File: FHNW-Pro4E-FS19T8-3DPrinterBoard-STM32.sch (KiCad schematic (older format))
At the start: 8 parts, among them J101 Screw_Terminal_01x02, U101 LM2675M-3.3

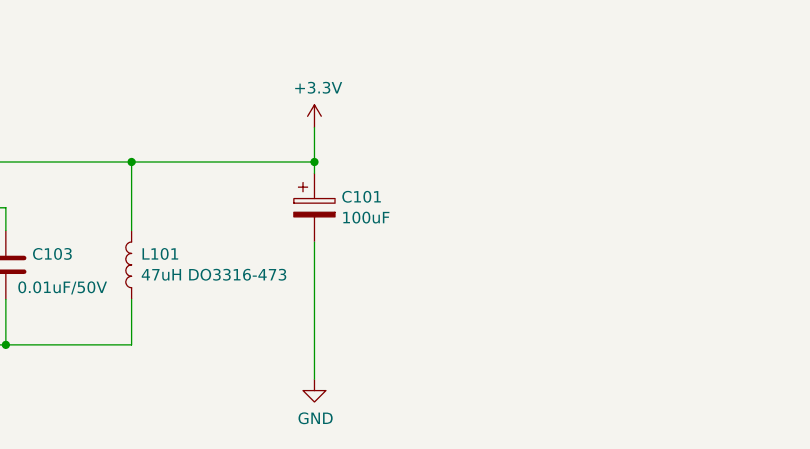
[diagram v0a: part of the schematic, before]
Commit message: added LEDs
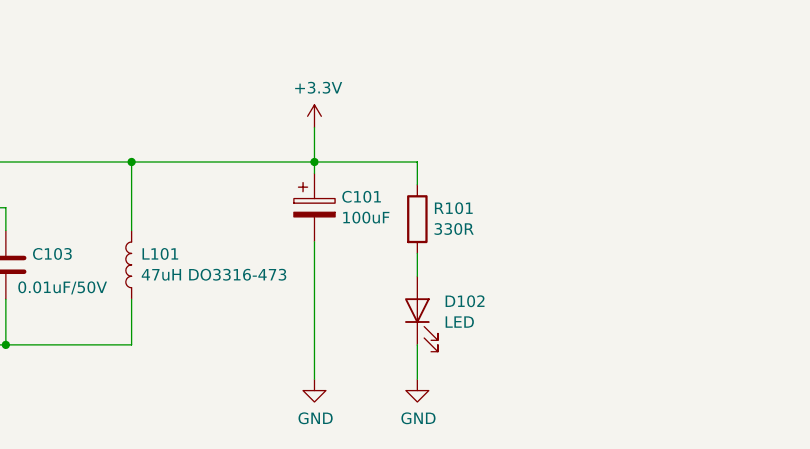
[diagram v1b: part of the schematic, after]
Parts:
- added D102: LED, LED_SMD:LED_0805_2012Metric, symbol Device:LED
- added R101: 330R, Resistors_SMD:R_0603, symbol Device:R
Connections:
- net +3V3: now also R101.1
- net GND: now also D102.1 (K)
- new net: D102.2 (A), R101.2
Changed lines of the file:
@@
 Wire Wire Line
 	2200 7250 2900 7250
+$Comp
+L Device:R R101
+U 1 1 5CB6A127
+P 5400 6700
+F 0 "R101" H 5470 6746 50  0000 L CNN
+F 1 "330R" H 5470 6655 50  0000 L CNN
+F 2 "Resistors_SMD:R_0603" V 5330 6700 50  0001 C CNN
+F 3 "~" H 5400 6700 50  0001 C CNN
+	1    5400 6700
+	1    0    0    -1
+$EndComp
+$Comp
+L Device:LED D102
+U 1 1 5CB6AB63
+P 5400 7100
+F 0 "D102" V 5439 6983 50  0000 R CNN
+F 1 "LED" V 5348 6983 50  0000 R CNN
+F 2 "LED_SMD:LED_0805_2012Metric" H 5400 7100 50  0001 C CNN
+F 3 "~" H 5400 7100 50  0001 C CNN
+	1    5400 7100
+	0    -1   -1   0
+$EndComp
+Wire Wire Line
+	4950 6450 5400 6450
+$Comp
+L power:GND #PWR0141
+U 1 1 5CB6C2A7
+P 5400 7400
+F 0 "#PWR0141" H 5400 7150 50  0001 C CNN
+F 1 "GND" H 5405 7227 50  0000 C CNN
+F 2 "" H 5400 7400 50  0001 C CNN
+F 3 "" H 5400 7400 50  0001 C CNN
+	1    5400 7400
+	1    0    0    -1
+$EndComp
+Wire Wire Line
+	5400 6450 5400 6550
+Wire Wire Line
+	5400 6850 5400 6950
+Wire Wire Line
+	5400 7250 5400 7400
 $EndSCHEMATC

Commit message: corrected P.S. Schematic review
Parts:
- added C104, C105, C106: 100n, Capacitors_SMD:C_0603, symbol Device:C
- added C107: 100uF, Capacitors_SMD:C_1812, symbol Device:CP
- added C108: 330uF, Capacitors_SMD:C_1812, symbol Device:CP
- added C109: 0.01uF/50V, Capacitors_SMD:C_0603, symbol Device:C
- added D103: Shottky STPS1L30A, Diodes_SMD:D_SMB, symbol Device:D_Schottky
- added FB101, FB102: Ferrite, Resistors_SMD:R_0805_HandSoldering, symbol Device:Ferrite_Bead_Small
- added L102: 47uH DO3316-473, Inductors_SMD:L_Fastron_PISN_Handsoldering, symbol Device:L
- added U102: LM2675M-5, Package_SO:SOIC-8_3.9x4.9mm_P1.27mm, symbol Regulator_Switching:LM2675M-5
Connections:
- net labels added: +3.3VA, +3.3VP, 5V
- wire segments 32 -> 74
- no-connect marks 1 -> 0
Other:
- note added: "Layout Datasheet p. 25"

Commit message: fixed missing symbol issue fixed 3vout cap on FTDI
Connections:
- net labels added: +5V
- net labels removed: 5V
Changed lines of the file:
@@
 Wire Wire Line
 	2300 6450 2200 6450
+Text Notes 4250 6000 2    50   ~ 0
+Layout Datasheet p. 25
 $Comp
-L SparkFun-PowerSymbols:5V #SUPPLY0101
-U 1 1 5CC53E98
+L power:+5V #PWR01
+U 1 1 5CBDFC0C
 P 4950 4650
-F 0 "#SUPPLY0101" H 5000 4650 45  0001 L BNN
-F 1 "5V" H 4950 4820 45  0000 C CNN
-F 2 "XXX-00000" H 4950 4831 60  0001 C CNN
-F 3 "" H 4950 4650 60  0001 C CNN
+F 0 "#PWR01" H 4950 4500 50  0001 C CNN
+F 1 "+5V" H 4965 4823 50  0000 C CNN
+F 2 "" H 4950 4650 50  0001 C CNN
+F 3 "" H 4950 4650 50  0001 C CNN
 	1    4950 4650
 	1    0    0    -1
 $EndComp
-Text Notes 4250 6000 2    50   ~ 0
-Layout Datasheet p. 25
 $EndSCHEMATC

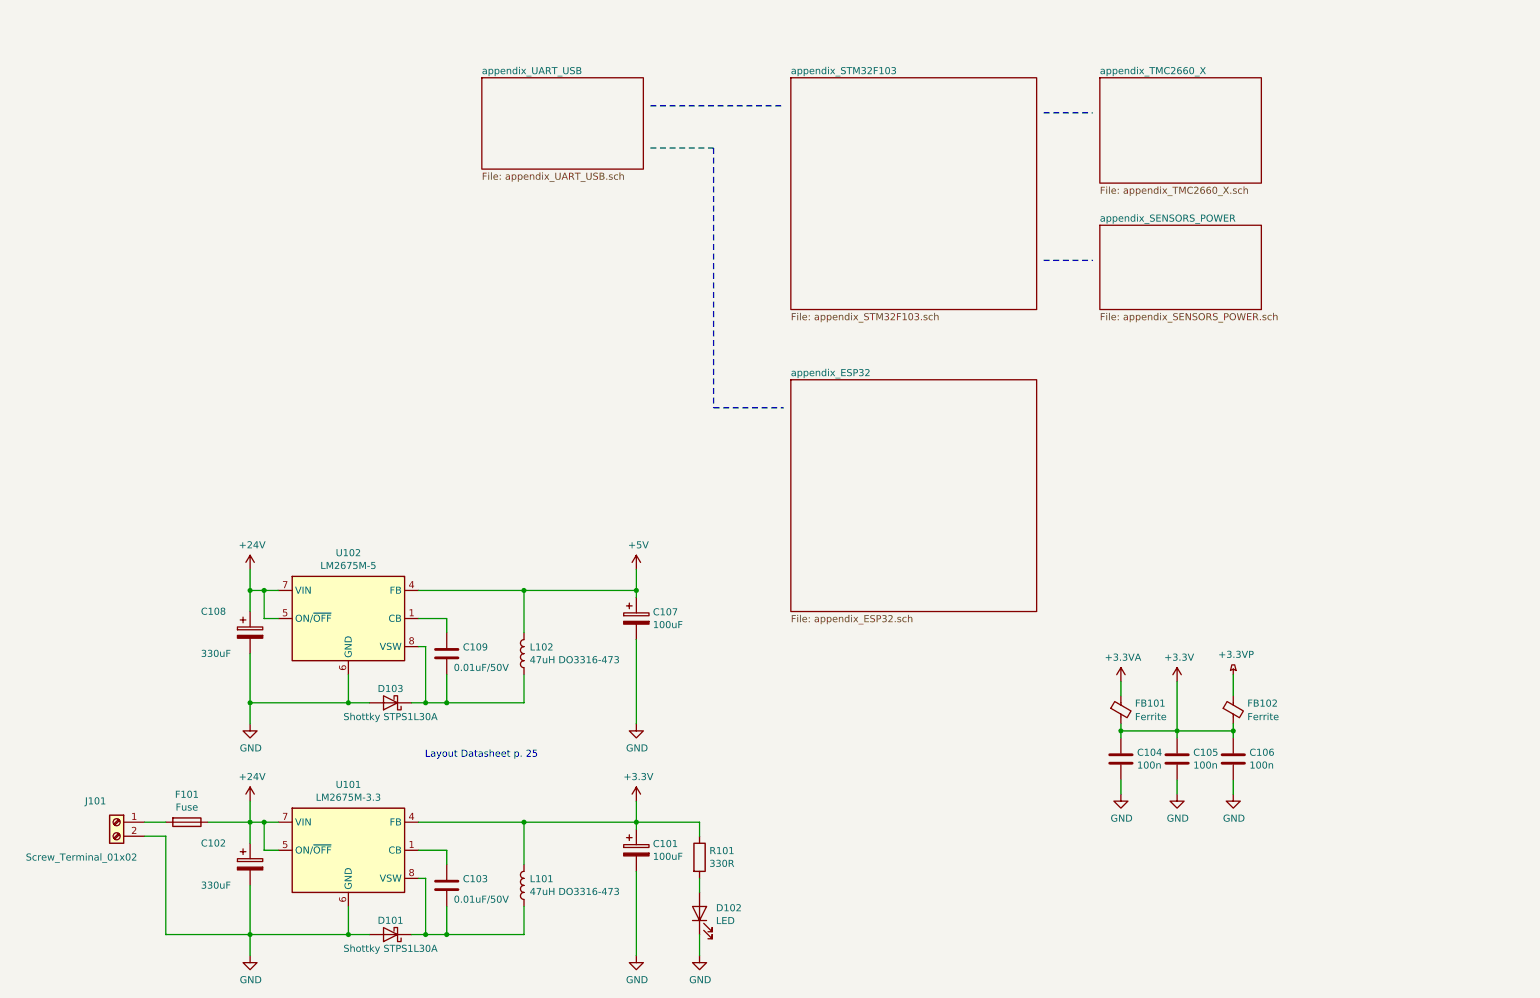
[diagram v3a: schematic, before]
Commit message: started with STM32 Pinout connections (Mittagspause)
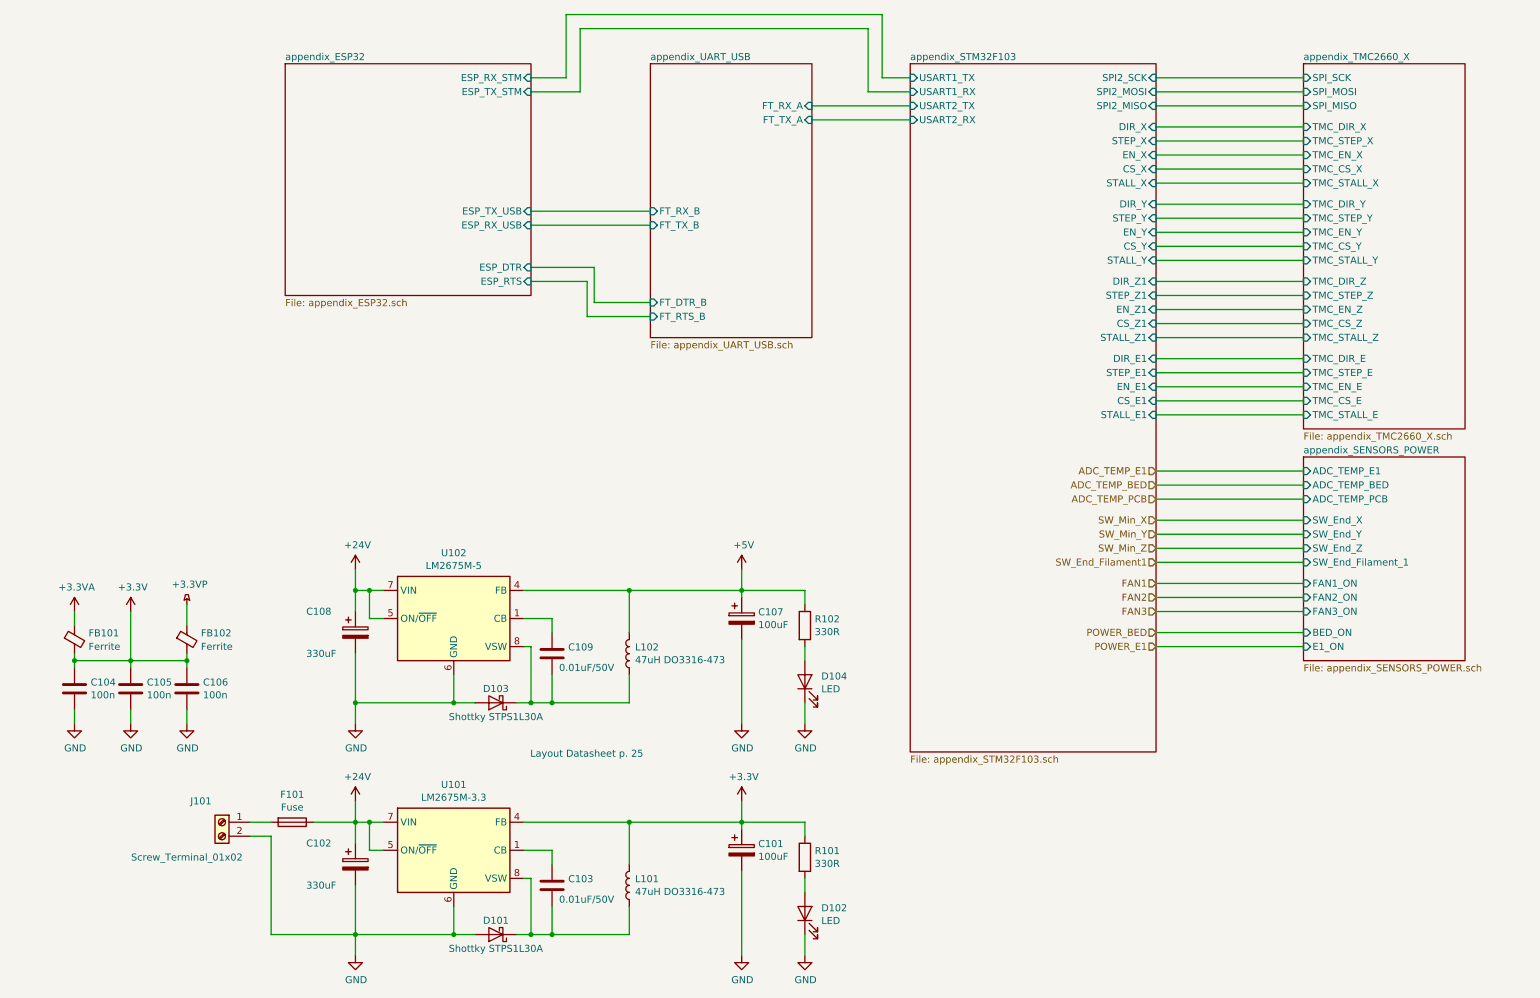
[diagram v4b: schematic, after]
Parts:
- added D104: LED, LED_SMD:LED_0805_2012Metric, symbol Device:LED
- added R102: 330R, Resistors_SMD:R_0603, symbol Device:R
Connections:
- net +5V: now also R102.1
- net GND: now also D104.1 (K)
- new net: D104.2 (A), R102.2
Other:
- moved on the sheet: C101, C102, C103, C104, C105, C106, C107, C108, C109, D101, D102, D103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

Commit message: added cache.lib to git
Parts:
- U101: footprint Housings_SOIC:SOIC-8-1EP_3.9x4.9mm_Pitch1.27mm -> Package_SO:SOIC-8_3.9x4.9mm_P1.27mm
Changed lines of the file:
@@
 F 0 "U101" H 3650 7117 50  0000 C CNN
 F 1 "LM2675M-3.3" H 3650 7026 50  0000 C CNN
-F 2 "Housings_SOIC:SOIC-8-1EP_3.9x4.9mm_Pitch1.27mm" H 3700 6300 50  0001 L CIN
+F 2 "Package_SO:SOIC-8_3.9x4.9mm_P1.27mm" H 3700 6300 50  0001 L CIN
 F 3 "http://www.ti.com/lit/ds/symlink/lm2675.pdf" H 3650 6650 50  0001 C CNN
 	1    3650 6650
@@
 Wire Wire Line
 	6150 5600 6150 5750
-Wire Wire Line
-	4200 2600 4600 2600
-Wire Wire Line
-	4600 2600 4600 2850
-Wire Wire Line
-	4600 2850 5050 2850
 Wire Wire Line
 	5050 2750 4650 2750
@@
 Text HLabel 8650 5200 0    50   Input ~ 0
 POWER_E1
+Wire Wire Line
+	4200 2600 4550 2600
+Wire Wire Line
+	4550 2600 4550 2850
+Wire Wire Line
+	4550 2850 5050 2850
 $EndSCHEMATC

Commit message: Layout update
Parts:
- added H101, H102, H103, H104: MountingHole, Mounting_Holes:MountingHole_3.2mm_M3_Pad, symbol Mechanical:MountingHole
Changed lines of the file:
@@
 Wire Wire Line
 	4550 2850 5050 2850
+$Comp
+L Mechanical:MountingHole H101
+U 1 1 5CBF1F93
+P 850 750
+F 0 "H101" H 950 700 50  0000 L CNN
+F 1 "MountingHole" H 600 600 50  0000 L CNN
+F 2 "Mounting_Holes:MountingHole_3.2mm_M3_Pad" H 850 750 50  0001 C CNN
+F 3 "~" H 850 750 50  0001 C CNN
+	1    850  750
+	1    0    0    -1
+$EndComp
+$Comp
+L Mechanical:MountingHole H102
+U 1 1 5CBF3649
+P 1400 750
+F 0 "H102" H 1500 700 50  0000 L CNN
+F 1 "MountingHole" H 1150 600 50  0000 L CNN
+F 2 "Mounting_Holes:MountingHole_3.2mm_M3_Pad" H 1400 750 50  0001 C CNN
+F 3 "~" H 1400 750 50  0001 C CNN
+	1    1400 750
+	1    0    0    -1
+$EndComp
+$Comp
+L Mechanical:MountingHole H103
+U 1 1 5CBF3A09
+P 850 1050
+F 0 "H103" H 950 1000 50  0000 L CNN
+F 1 "MountingHole" H 600 900 50  0000 L CNN
+F 2 "Mounting_Holes:MountingHole_3.2mm_M3_Pad" H 850 1050 50  0001 C CNN
+F 3 "~" H 850 1050 50  0001 C CNN
+	1    850  1050
+	1    0    0    -1
+$EndComp
+$Comp
+L Mechanical:MountingHole H104
+U 1 1 5CBF3E8E
+P 1400 1050
+F 0 "H104" H 1500 1000 50  0000 L CNN
+F 1 "MountingHole" H 1150 900 50  0000 L CNN
+F 2 "Mounting_Holes:MountingHole_3.2mm_M3_Pad" H 1400 1050 50  0001 C CNN
+F 3 "~" H 1400 1050 50  0001 C CNN
+	1    1400 1050
+	1    0    0    -1
+$EndComp
 $EndSCHEMATC

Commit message: having issues with netclasses
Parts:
- added C110: TBD, Capacitors_SMD:C_0603, symbol Device:C
- added D105: D_Zener, Diodes_SMD:D_SMB, symbol Device:D_Zener
- added R103: TBD, Resistors_SMD:R_0603, symbol Device:R
- added T101: BUK963R3-60E, Package_TO_SOT_SMD:TO-263-2, symbol FHNW-Pro4E-FS19T8-Library:BUK963R3-60E
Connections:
- net GND: now also D105.2 (A), T101.3; no longer J101.2 (Pin_2)
- net at J101.1 (Pin_1): now also T101.2; no longer F101.2
- new net: C110.2, D105.1 (K), R103.2, T101.1
- new net: C110.1, F101.2, J101.2 (Pin_2), R103.1
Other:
- moved on the sheet: C104, C105, C106, FB101, FB102, J101

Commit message: first layout draft without 40pin
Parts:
- added D106: APHBM2012LSURKZGKC, FHNW-Pro4E-FS19T8-Library:LED_Kingbright_SMD4_2.0x1.25, symbol FHNW-Pro4E-FS19T8-Library:APHBM2012LSURKZGKC
- added R104: 10k, Resistors_SMD:R_1206, symbol Device:R
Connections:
- net 24V_GND: now reaches J101.1 (Pin_1), T101.2
- net 24V_GND: now also D106.1 (A1), D106.3 (K2)
- net 24V_IN: now reaches C110.1, F101.2, J101.2 (Pin_2), R103.1
- net 24V_IN: now also R104.1
- new net: D106.2 (K1), D106.4 (A2), R104.2
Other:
- moved on the sheet: J101
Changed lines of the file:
@@
 F27 "CS_E1" I R 8650 3450 50
 F28 "STALL_E1" I R 8650 3550 50
+F29 "ADC_T_E1" I R 8650 3950 50
+F30 "ADC_T_BED" I R 8650 4050 50
+F31 "BED_ON" I R 8650 5100 50
+F32 "E1_ON" I R 8650 5200 50
+F33 "FAN1" I R 8650 4750 50
+F34 "FAN2" I R 8650 4850 50
+F35 "FAN3" I R 8650 4950 50
+F36 "ADC_T_PCB" I R 8650 4150 50
+F37 "SW_Min_X" I R 8650 4300 50
+F38 "SW_Min_Y" I R 8650 4400 50
+F39 "SW_Min_Z1" I R 8650 4500 50
+F40 "SW_Min_Filament1" I R 8650 4600 50
 $EndSheet
 $Sheet
@@
 L Connector:Screw_Terminal_01x02 J101
 U 1 1 5CD68AD6
-P 1250 6550
-F 0 "J101" H 1400 6700 50  0000 C CNN
-F 1 "Screw_Terminal_01x02" H 1500 6300 50  0000 C CNN
-F 2 "Connectors_Terminal_Blocks:TerminalBlock_Altech_AK300-2_P5.00mm" H 1250 6550 50  0001 C CNN
-F 3 "~" H 1250 6550 50  0001 C CNN
-	1    1250 6550
+P 650 6550
+F 0 "J101" H 600 6700 50  0000 C CNN
+F 1 "Screw_Terminal_01x02" V 750 6200 50  0000 C CNN
+F 2 "Connectors_Terminal_Blocks:TerminalBlock_Altech_AK300-2_P5.00mm" H 650 6550 50  0001 C CNN
+F 3 "~" H 650 6550 50  0001 C CNN
+	1    650  6550
 	-1   0    0    1
 $EndComp
@@
 $EndComp
 $Comp
-L Device:C C105
-U 1 1 5CC01495
-P 1400 4150
-F 0 "C105" H 1515 4196 50  0000 L CNN
-F 1 "100n" H 1515 4105 50  0000 L CNN
-F 2 "Capacitors_SMD:C_0603" H 1438 4000 50  0001 C CNN
-F 3 "~" H 1400 4150 50  0001 C CNN
-	1    1400 4150
-	1    0    0    -1
-$EndComp
-$Comp
 L power:GND #PWR0126
 U 1 1 5CC014A2
@@
 Wire Wire Line
 	9700 4950 8650 4950
-Text HLabel 8650 4050 0    50   Input ~ 0
-ADC_T_BED
-Text HLabel 8650 3950 0    50   Input ~ 0
-ADC_T_E1
-Text HLabel 8650 4300 0    50   Input ~ 0
-SW_Min_X
-Text HLabel 8650 4400 0    50   Input ~ 0
-SW_Min_Y
-Text HLabel 8650 4500 0    50   Input ~ 0
-SW_Min_Z
-Text HLabel 8650 4600 0    50   Input ~ 0
-SW_End_Filament1
-Text HLabel 8650 4750 0    50   Input ~ 0
-FAN1
-Text HLabel 8650 4850 0    50   Input ~ 0
-FAN2
-Text HLabel 8650 4950 0    50   Input ~ 0
-FAN3
-Text HLabel 8650 5100 0    50   Input ~ 0
-BED_ON
-Text HLabel 8650 5200 0    50   Input ~ 0
-E1_ON
 Wire Wire Line
 	4200 2600 4550 2600
@@
 Wire Wire Line
 	1900 6450 2250 6450
-Wire Wire Line
-	1450 6450 1900 6450
-Connection ~ 1900 6450
-Wire Wire Line
-	1700 7250 1550 7250
-Wire Wire Line
-	1550 7250 1550 6550
-Wire Wire Line
-	1550 6550 1450 6550
 $Comp
 L Device:D_Zener D105
@@
 	0    1    1    0
 $EndComp
-Text HLabel 8650 4150 0    50   Input ~ 0
-ADC_T_PCB
 $Sheet
 S 9700 3850 1150 1450
@@
 Wire Wire Line
 	9700 5200 8650 5200
+Text Label 950  6950 1    50   ~ 0
+24V_GND
+Text Label 1900 6450 0    50   ~ 0
+24V_IN
+$Comp
+L Device:R R104
+U 1 1 5CC041F6
+P 1450 6300
+F 0 "R104" H 1520 6346 50  0000 L CNN
+F 1 "10k" H 1520 6255 50  0000 L CNN
+F 2 "Resistors_SMD:R_1206" V 1380 6300 50  0001 C CNN
+F 3 "~" H 1450 6300 50  0001 C CNN
+	1    1450 6300
+	1    0    0    -1
+$EndComp
+$Comp
+L FHNW-Pro4E-FS19T8-Library:APHBM2012LSURKZGKC D106
+U 1 1 5CC0EDCA
+P 1350 6850
+F 0 "D106" V 1304 6640 50  0000 R CNN
+F 1 "APHBM2012LSURKZGKC" V 1395 6640 50  0000 R CNN
+F 2 "FHNW-Pro4E-FS19T8-Library:LED_Kingbright_SMD4_2.0x1.25" H 1380 6850 50  0001 C CNN
+F 3 "~" H 1380 6850 50  0001 C CNN
+	1    1350 6850
+	0    -1   1    0
+$EndComp
+Wire Wire Line
+	950  7250 950  6550
+Wire Wire Line
+	950  6550 850  6550
+Wire Wire Line
+	950  7250 1450 7250
+Wire Wire Line
+	1450 7150 1450 7250
+Connection ~ 1450 7250
+Wire Wire Line
+	1450 7250 1700 7250
+Wire Wire Line
+	950  6550 1250 6550
+Connection ~ 950  6550
+Wire Wire Line
+	1250 7150 1250 7200
+Wire Wire Line
+	1250 7200 1600 7200
+Wire Wire Line
+	1600 7200 1600 6500
+Wire Wire Line
+	1600 6500 1450 6500
+Wire Wire Line
+	1450 6500 1450 6550
+Wire Wire Line
+	850  6450 950  6450
+Wire Wire Line
+	950  6450 950  6100
+Wire Wire Line
+	950  6100 1450 6100
+Wire Wire Line
+	1800 6100 1800 6450
+Wire Wire Line
+	1800 6450 1900 6450
+Connection ~ 1900 6450
+Wire Wire Line
+	1450 6450 1450 6500
+Connection ~ 1450 6500
+Wire Wire Line
+	1450 6150 1450 6100
+Connection ~ 1450 6100
+Wire Wire Line
+	1450 6100 1800 6100
+$Comp
+L Device:C C105
+U 1 1 5CC01495
+P 1400 4150
+F 0 "C105" H 1515 4196 50  0000 L CNN
+F 1 "100n" H 1515 4105 50  0000 L CNN
+F 2 "Capacitors_SMD:C_0603" H 1438 4000 50  0001 C CNN
+F 3 "~" H 1400 4150 50  0001 C CNN
+	1    1400 4150
+	1    0    0    -1
+$EndComp
 $EndSCHEMATC
